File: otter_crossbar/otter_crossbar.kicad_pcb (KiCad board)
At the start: 4 copper layers, 166 x 19 mm, 13 parts, among them J1 Conn_02x12_Counter_Clockwise, J2 Conn_02x12_Counter_Clockwise, J3 Conn_02x12_Counter_Clockwise, J4 Conn_02x08_Odd_Even, J5 Conn_02x08_Odd_Even

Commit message: wip on crossbars
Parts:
- added J6: Conn_02x20_Odd_Even, custom:Samtec_MECF-20-0_-NP-L-DV_2x20_P1.27mm_Edge_mod, F.Cu at (0.00, -5.00)
- J4, J5: value Conn_02x08_Odd_Even -> Conn_02x12_Counter_Clockwise; footprint custom:Samtec_MECF-08-0_-NP-L-DV_2x08_P1.27mm_Edge_mod -> custom:PinSocket_2x12_P2.00mm_Vertical_EDGE
- moved J4 100.9 mm to (29.0, -19.9)
- moved J3 42.5 mm to (0.00, -19.9)
- moved J2 29.0 mm to (-29.0, -19.9)
- moved J5 19.7 mm to (58.0, -19.9)
- moved J1 15.5 mm to (-58.0, -19.9)
- moved H1 11.7 mm to (-91.7, -26.0)
- moved H2 11.7 mm to (-91.7, -13.0)
- moved H3 11.7 mm to (91.7, -26.0)
- moved H4 11.7 mm to (91.7, -13.0)
- moved JP1 11.7 mm to (-87.0, -25.9)
- moved JP2 11.7 mm to (-93.2, -18.9)
- moved JP3 11.7 mm to (87.2, -26.9)
- moved JP4 11.7 mm to (92.2, -18.4)
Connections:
- J1 pad 1: /C1 -> /E1
- J1 pad 11: /C6 -> /E6
- J1 pad 13: /C7 -> /E7
- J1 pad 17: /C9 -> /E9
- J1 pad 19: /C10 -> /E10
- J1 pad 21: /C11 -> /E2
- J1 pad 23: /C12 -> /E1
- J1 pad 3: /C2 -> /E2
- J1 pad 5: /C3 -> /E3
- J1 pad 7: /C4 -> /E4
- J2 pad 1: /B1 -> /D1
- J2 pad 11: /B6 -> /D6
- J2 pad 13: /B7 -> /D7
- J2 pad 17: /B9 -> /D9
- J2 pad 19: /B10 -> /D10
- J2 pad 21: /B11 -> /D2
- J2 pad 23: /B12 -> /D1
- J2 pad 3: /B2 -> /D2
- J2 pad 5: /B3 -> /D3
- J2 pad 7: /B4 -> /D4
- J3 pad 1: /A1 -> /C1
- J3 pad 11: /A6 -> /C6
- J3 pad 13: /A7 -> /C7
- J3 pad 17: /A9 -> /C9
- J3 pad 19: /A10 -> /C10
- J3 pad 21: /A11 -> /C2
- J3 pad 23: /A12 -> /C1
- J3 pad 3: /A2 -> /C2
- J3 pad 5: /A3 -> /C3
- J3 pad 7: /A4 -> /C4
- J4 pad 1: GND -> /B1
- J4 pad 10: /C7 -> (no net)
- J4 pad 11: /B12 -> /B6
- J4 pad 12: /C6 -> (no net)
- J4 pad 13: /C1 -> /B7
- J4 pad 14: /C4 -> (no net)
- J4 pad 15: /C2 -> (no net)
- J4 pad 16: /C3 -> (no net)
- J4 pad 2: /C12 -> (no net)
- J4 pad 3: /B7 -> /B2
- J4 pad 4: /C11 -> (no net)
- J4 pad 5: /B9 -> /B3
- J4 pad 6: /C10 -> (no net)
- J4 pad 7: /B10 -> /B4
- J4 pad 8: /C9 -> (no net)
- J4 pad 9: /B11 -> (no net)
- J5 pad 1: /A11 -> /A1
- J5 pad 10: /A4 -> (no net)
- J5 pad 11: /B4 -> /A6
- J5 pad 12: /A3 -> (no net)
- J5 pad 13: /B6 -> /A7
- J5 pad 14: /A2 -> (no net)
- J5 pad 15: GND -> (no net)
- J5 pad 16: /A1 -> (no net)
- J5 pad 2: /A10 -> (no net)
- J5 pad 3: /A12 -> /A2
- J5 pad 4: /A9 -> (no net)
- J5 pad 5: /B1 -> /A3
- J5 pad 6: /A7 -> (no net)
- J5 pad 7: /B2 -> /A4
- J5 pad 8: /A6 -> (no net)
- J5 pad 9: /B3 -> (no net)
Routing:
- net /E2: track 0.00 -> 96.2 mm, vias 0 -> 3
- net /E1: track 0.00 -> 93.0 mm, vias 0 -> 4
- net /B11: track 77.2 -> 0.00 mm, vias 2 -> 0
- net /B12: track 72.6 -> 0.00 mm, vias 2 -> 0
- net /D2: track 0.00 -> 67.8 mm, vias 0 -> 3
- net GND: track 182.1 -> 114.5 mm, vias 1 -> 6
- net /E10: track 0.00 -> 65.0 mm, vias 0 -> 2
- net /E9: track 0.00 -> 64.5 mm, vias 0 -> 2
- net /E7: track 0.00 -> 63.6 mm, vias 0 -> 2
- net /E6: track 0.00 -> 63.4 mm, vias 0 -> 2
- net /D1: track 0.00 -> 63.1 mm, vias 0 -> 4
- net /E4: track 0.00 -> 59.3 mm, vias 0 -> 2
- net /E3: track 0.00 -> 59.1 mm, vias 0 -> 2
- net /C3: track 75.9 -> 16.8 mm, vias 2 -> 1
- net /B6: track 93.1 -> 37.6 mm
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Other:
- board size 166 x 19 mm -> 189.4 x 19 mm

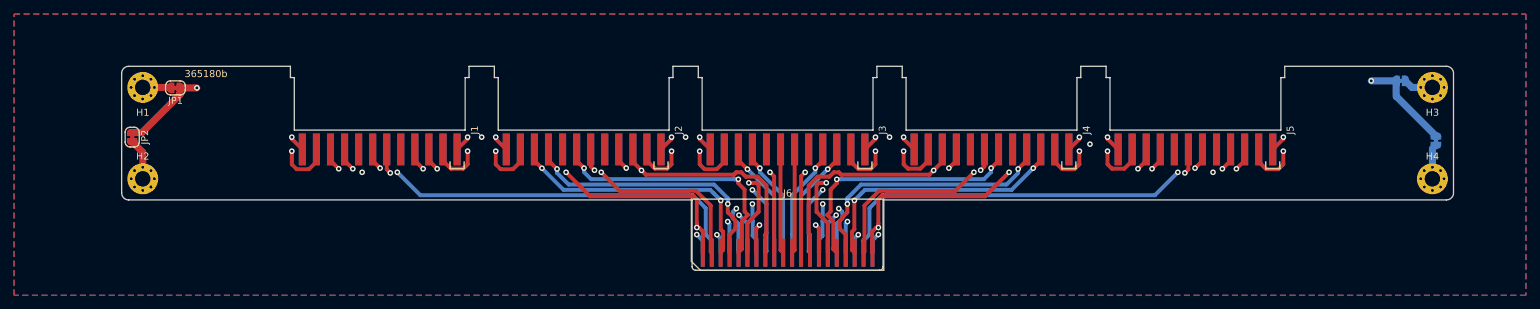
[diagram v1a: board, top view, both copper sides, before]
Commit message: otter crossbars shortened
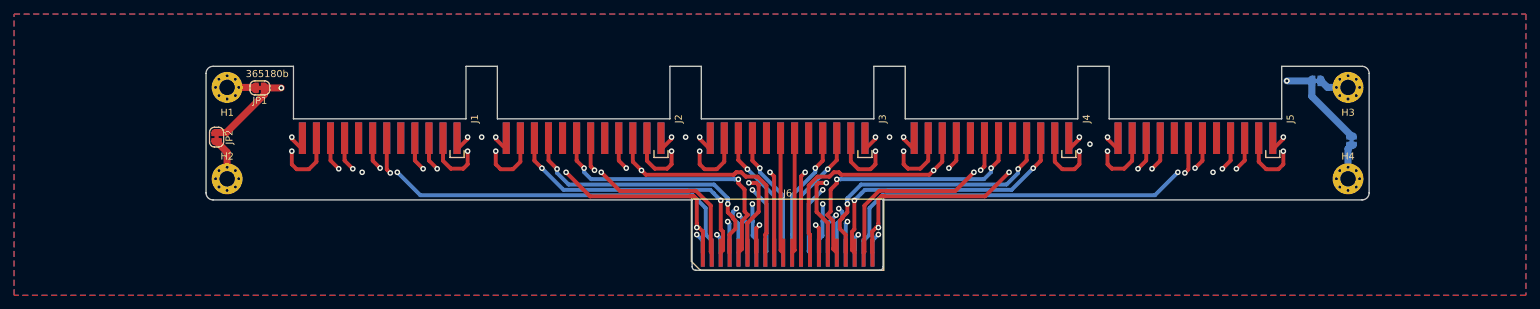
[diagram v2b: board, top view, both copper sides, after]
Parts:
- moved H1 12.0 mm to (-79.7, -26.0)
- moved H2 12.0 mm to (-79.7, -13.0)
- moved H3 12.0 mm to (79.7, -26.0)
- moved H4 12.0 mm to (79.7, -13.0)
- moved JP1 12.0 mm to (-75.0, -25.9)
- moved JP2 12.0 mm to (-81.2, -18.9)
- moved JP3 12.0 mm to (75.2, -26.9)
- moved JP4 12.0 mm to (80.2, -18.4)
- moved J1 1.60 mm to (-58.0, -21.5)
- moved J2 1.60 mm to (-29.0, -21.5)
- moved J3 1.60 mm to (0.00, -21.5)
- moved J4 1.60 mm to (29.0, -21.5)
- moved J5 1.60 mm to (58.0, -21.5)
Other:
- board size 189.4 x 19 mm -> 165.4 x 19 mm

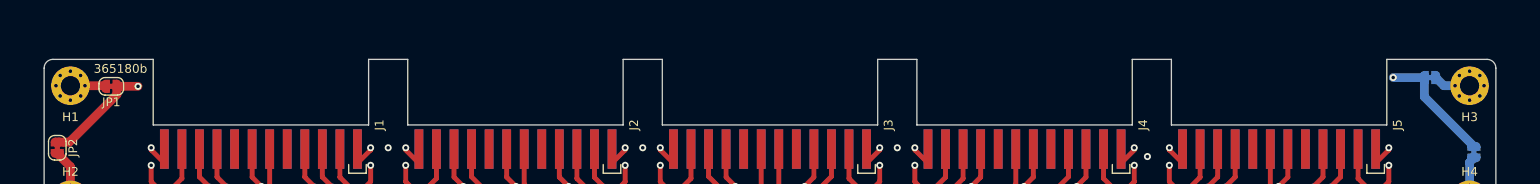
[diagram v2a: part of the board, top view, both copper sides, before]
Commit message: otter crossbar modified
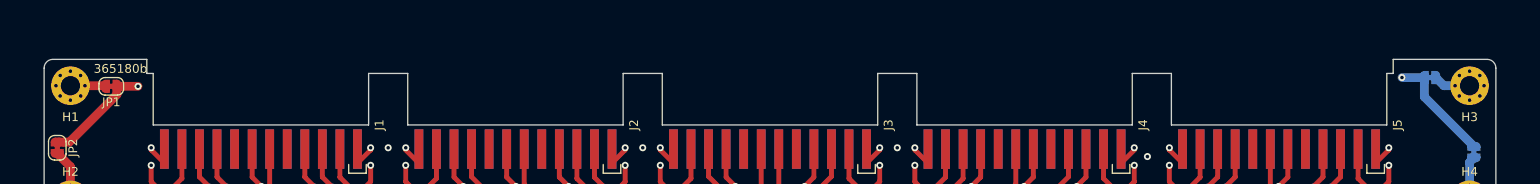
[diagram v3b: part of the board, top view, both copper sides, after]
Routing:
- net GND: track 114.5 -> 113.5 mm
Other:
- outline, holes or cut-outs redrawn
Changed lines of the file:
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@@
   (general
     (thickness 1.6)
-    (drawings 28)
+    (drawings 32)
     (tracks 631)
     (zones 0)
@@
       (net 38 /D1))
   )
+  (gr_line (start 71 -27.4) (end 71 -29) (layer Edge.Cuts) (width 0.05))
+  (gr_line (start -71 -29) (end -71 -27.4) (layer Edge.Cuts) (width 0.05))
+  (gr_line (start 70.27 -27.4) (end 71 -27.4) (layer Edge.Cuts) (width 0.05))
+  (gr_line (start -70.27 -27.4) (end -71 -27.4) (layer Edge.Cuts) (width 0.05))
   (gr_line (start -81.7 -10) (end -13.575 -10) (layer Edge.Cuts) (width 0.05))
-  (gr_line (start -70.27 -29) (end -81.7 -29) (layer Edge.Cuts) (width 0.05))
+  (gr_line (start -71 -29) (end -81.7 -29) (layer Edge.Cuts) (width 0.05))
   (gr_line (start 81.7 -10) (end 13.575 -10) (layer Edge.Cuts) (width 0.05))
-  (gr_line (start 70.27 -29) (end 81.7 -29) (layer Edge.Cuts) (width 0.05))
+  (gr_line (start 71 -29) (end 81.7 -29) (layer Edge.Cuts) (width 0.05))
   (gr_line (start 113 -9.5) (end -115 -9.5) (layer Dwgs.User) (width 0.15))
   (gr_line (start 113 2.5) (end -115 2.5) (layer Dwgs.User) (width 0.15))
-  (gr_line (start -45.73 -29) (end -41.27 -29) (layer Edge.Cuts) (width 0.05))
-  (gr_line (start -70.27 -21.53) (end -70.27 -29) (layer Edge.Cuts) (width 0.05))
-  (gr_line (start -45.73 -21.53) (end -45.73 -29) (layer Edge.Cuts) (width 0.05))
-  (gr_line (start 45.73 -21.53) (end 45.73 -29) (layer Edge.Cuts) (width 0.05))
-  (gr_line (start 41.27 -29) (end 45.73 -29) (layer Edge.Cuts) (width 0.05))
-  (gr_line (start 70.27 -21.53) (end 70.27 -29) (layer Edge.Cuts) (width 0.05))
-  (gr_line (start 16.73 -21.53) (end 16.73 -29) (layer Edge.Cuts) (width 0.05))
-  (gr_line (start 12.27 -29) (end 16.73 -29) (layer Edge.Cuts) (width 0.05))
-  (gr_line (start 41.27 -21.53) (end 41.27 -29) (layer Edge.Cuts) (width 0.05))
-  (gr_line (start -41.27 -21.53) (end -41.27 -29) (layer Edge.Cuts) (width 0.05))
-  (gr_line (start -16.73 -21.53) (end -16.73 -29) (layer Edge.Cuts) (width 0.05))
+  (gr_line (start -45.73 -27.4) (end -41.27 -27.4) (layer Edge.Cuts) (width 0.05))
+  (gr_line (start -70.27 -21.53) (end -70.27 -27.4) (layer Edge.Cuts) (width 0.05))
+  (gr_line (start -45.73 -21.53) (end -45.73 -27.4) (layer Edge.Cuts) (width 0.05))
+  (gr_line (start 45.73 -21.53) (end 45.73 -27.4) (layer Edge.Cuts) (width 0.05))
+  (gr_line (start 41.27 -27.4) (end 45.73 -27.4) (layer Edge.Cuts) (width 0.05))
+  (gr_line (start 70.27 -21.53) (end 70.27 -27.4) (layer Edge.Cuts) (width 0.05))
+  (gr_line (start 16.73 -21.53) (end 16.73 -27.4) (layer Edge.Cuts) (width 0.05))
+  (gr_line (start 12.27 -27.4) (end 16.73 -27.4) (layer Edge.Cuts) (width 0.05))
+  (gr_line (start 41.27 -21.53) (end 41.27 -27.4) (layer Edge.Cuts) (width 0.05))
+  (gr_line (start -41.27 -21.53) (end -41.27 -27.4) (layer Edge.Cuts) (width 0.05))
+  (gr_line (start -16.73 -21.53) (end -16.73 -27.4) (layer Edge.Cuts) (width 0.05))
   (gr_text 365180b (at -74 -27.93) (layer B.SilkS)
     (effects (font (size 1 1) (thickness 0.15)) (justify mirror))
@@
   (gr_arc (start 81.7 -11) (end 81.7 -10) (angle -90) (layer Edge.Cuts) (width 0.05))
   (gr_line (start 82.7 -11) (end 82.7 -28) (layer Edge.Cuts) (width 0.05))
-  (gr_line (start 12.27 -21.53) (end 12.27 -29) (layer Edge.Cuts) (width 0.05))
-  (gr_line (start -16.73 -29) (end -12.27 -29) (layer Edge.Cuts) (width 0.05))
-  (gr_line (start -12.27 -21.53) (end -12.27 -29) (layer Edge.Cuts) (width 0.05))
+  (gr_line (start 12.27 -21.53) (end 12.27 -27.4) (layer Edge.Cuts) (width 0.05))
+  (gr_line (start -16.73 -27.4) (end -12.27 -27.4) (layer Edge.Cuts) (width 0.05))
+  (gr_line (start -12.27 -21.53) (end -12.27 -27.4) (layer Edge.Cuts) (width 0.05))
   (gr_arc (start 81.7 -28) (end 82.7 -28) (angle -90) (layer Edge.Cuts) (width 0.05))
   (gr_arc (start -81.7 -28) (end -81.7 -29) (angle -90) (layer Edge.Cuts) (width 0.05))
@@
   (segment (start 80.2 -19.08) (end 74.55 -24.73) (width 1) (layer B.Cu) (net 29) (status 10))
   (via (at -72 -25.93) (size 0.8) (drill 0.4) (layers F.Cu B.Cu) (net 29))
-  (via (at 71 -26.93) (size 0.8) (drill 0.4) (layers F.Cu B.Cu) (net 29))
-  (segment (start 74.55 -26.93) (end 71 -26.93) (width 1) (layer B.Cu) (net 29) (status 10))
   (segment (start -72 -25.93) (end -74.4 -25.93) (width 1) (layer F.Cu) (net 29) (status 20))
   (via (at 43 -17.93) (size 0.8) (drill 0.4) (layers F.Cu B.Cu) (net 29))
@@
   (segment (start 15.5 -17.93) (end 43 -17.93) (width 0.56) (layer In2.Cu) (net 29))
   (segment (start 14.5 -18.93) (end 15.5 -17.93) (width 0.56) (layer In2.Cu) (net 29))
+  (segment (start 74.55 -26.93) (end 72 -26.93) (width 1) (layer B.Cu) (net 29))
+  (via (at 72 -26.93) (size 0.8) (drill 0.4) (layers F.Cu B.Cu) (net 29))
   (via (at -60.5 -13.93) (size 0.8) (drill 0.4) (layers F.Cu B.Cu) (net 30))
   (segment (start -70.5 -18.68) (end -69 -17.18) (width 0.56) (layer F.Cu) (net 30) (status 20))

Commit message: update silk
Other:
- board text added: "6c4861d"
- board text removed: "365180b"
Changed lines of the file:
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@@
   (gr_line (start -41.27 -21.53) (end -41.27 -27.4) (layer Edge.Cuts) (width 0.05))
   (gr_line (start -16.73 -21.53) (end -16.73 -27.4) (layer Edge.Cuts) (width 0.05))
-  (gr_text 365180b (at -74 -27.93) (layer B.SilkS)
+  (gr_text 6c4861d (at -74.5 -28) (layer B.SilkS)
     (effects (font (size 1 1) (thickness 0.15)) (justify mirror))
   )
-  (gr_text 365180b (at -74 -27.93) (layer F.SilkS)
+  (gr_text 6c4861d (at -74.5 -27.93) (layer F.SilkS)
     (effects (font (size 1 1) (thickness 0.15)))
   )

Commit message: start baseboard
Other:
- board text added: "A"
- board text added: "B"
- board text added: "C"
- board text added: "D"
- board text added: "E"
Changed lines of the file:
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@@
   (general
     (thickness 1.6)
-    (drawings 32)
+    (drawings 42)
     (tracks 631)
     (zones 0)
@@
       (effects (font (size 1 1) (thickness 0.15)))
     )
-    (fp_text value Conn_02x12_Counter_Clockwise (at -13.5 0 270) (layer F.Fab)
+    (fp_text value Conn_02x12_Counter_Clockwise (at -13.5 0 270) (layer F.Fab) hide
       (effects (font (size 1 1) (thickness 0.15)))
     )
@@
       (effects (font (size 1 1) (thickness 0.15)))
     )
-    (fp_text value Conn_02x12_Counter_Clockwise (at -13.5 0 270) (layer F.Fab)
+    (fp_text value Conn_02x12_Counter_Clockwise (at -13.5 0 270) (layer F.Fab) hide
       (effects (font (size 1 1) (thickness 0.15)))
     )
@@
     (tags "conn samtec card-edge high-speed")
     (attr virtual)
-    (fp_text reference J6 (at 0 -5.95) (layer F.SilkS)
+    (fp_text reference J6 (at -12.5 -6) (layer F.SilkS)
       (effects (font (size 1 1) (thickness 0.15)))
     )
@@
       (net 38 /D1))
   )
+  (gr_text E (at -58.5 -11.5) (layer B.SilkS)
+    (effects (font (size 1 1) (thickness 0.15)) (justify mirror))
+  )
+  (gr_text D (at -29 -11.5) (layer B.SilkS)
+    (effects (font (size 1 1) (thickness 0.15)) (justify mirror))
+  )
+  (gr_text C (at 0 -13) (layer B.SilkS)
+    (effects (font (size 1 1) (thickness 0.15)) (justify mirror))
+  )
+  (gr_text B (at 29.5 -12) (layer B.SilkS)
+    (effects (font (size 1 1) (thickness 0.15)) (justify mirror))
+  )
+  (gr_text A (at 58 -12) (layer B.SilkS)
+    (effects (font (size 1 1) (thickness 0.15)) (justify mirror))
+  )
+  (gr_text A (at 58 -12) (layer F.SilkS)
+    (effects (font (size 1 1) (thickness 0.15)))
+  )
+  (gr_text B (at 29.5 -12) (layer F.SilkS)
+    (effects (font (size 1 1) (thickness 0.15)))
+  )
+  (gr_text C (at 0 -13) (layer F.SilkS)
+    (effects (font (size 1 1) (thickness 0.15)))
+  )
+  (gr_text D (at -29 -11.5) (layer F.SilkS)
+    (effects (font (size 1 1) (thickness 0.15)))
+  )
+  (gr_text E (at -58.5 -11.5) (layer F.SilkS)
+    (effects (font (size 1 1) (thickness 0.15)))
+  )
   (gr_line (start 71 -27.4) (end 71 -29) (layer Edge.Cuts) (width 0.05))

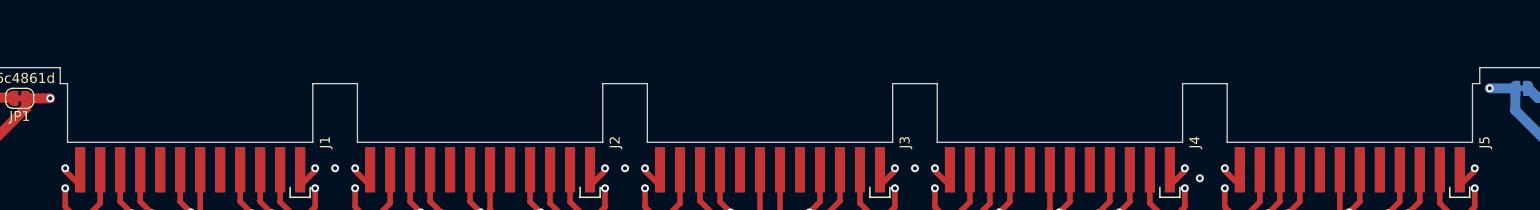
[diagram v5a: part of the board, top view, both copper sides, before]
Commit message: fix lim baseboard bug
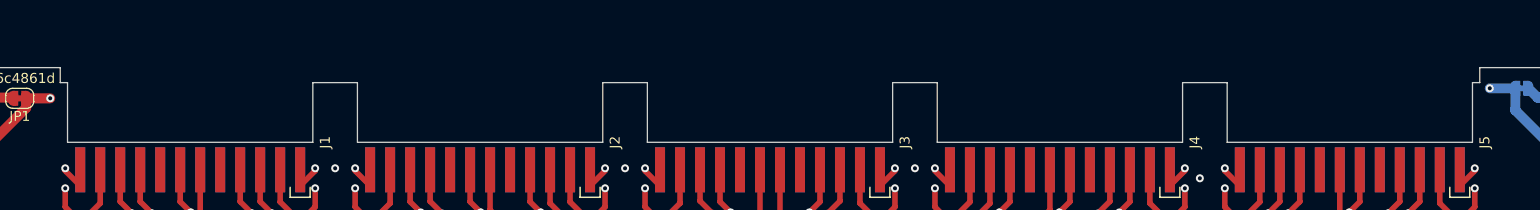
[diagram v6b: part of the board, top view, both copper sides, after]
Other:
- outline, holes or cut-outs redrawn
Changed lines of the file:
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@@
     (effects (font (size 1 1) (thickness 0.15)))
   )
-  (gr_line (start 71 -27.4) (end 71 -29) (layer Edge.Cuts) (width 0.05))
-  (gr_line (start -71 -29) (end -71 -27.4) (layer Edge.Cuts) (width 0.05))
-  (gr_line (start 70.27 -27.4) (end 71 -27.4) (layer Edge.Cuts) (width 0.05))
-  (gr_line (start -70.27 -27.4) (end -71 -27.4) (layer Edge.Cuts) (width 0.05))
+  (gr_line (start 71 -27.5) (end 71 -29) (layer Edge.Cuts) (width 0.05))
+  (gr_line (start -71 -29) (end -71 -27.5) (layer Edge.Cuts) (width 0.05))
+  (gr_line (start 70.27 -27.5) (end 71 -27.5) (layer Edge.Cuts) (width 0.05))
+  (gr_line (start -70.27 -27.5) (end -71 -27.5) (layer Edge.Cuts) (width 0.05))
   (gr_line (start -81.7 -10) (end -13.575 -10) (layer Edge.Cuts) (width 0.05))
   (gr_line (start -71 -29) (end -81.7 -29) (layer Edge.Cuts) (width 0.05))
@@
   (gr_line (start 113 -9.5) (end -115 -9.5) (layer Dwgs.User) (width 0.15))
   (gr_line (start 113 2.5) (end -115 2.5) (layer Dwgs.User) (width 0.15))
-  (gr_line (start -45.73 -27.4) (end -41.27 -27.4) (layer Edge.Cuts) (width 0.05))
-  (gr_line (start -70.27 -21.53) (end -70.27 -27.4) (layer Edge.Cuts) (width 0.05))
-  (gr_line (start -45.73 -21.53) (end -45.73 -27.4) (layer Edge.Cuts) (width 0.05))
-  (gr_line (start 45.73 -21.53) (end 45.73 -27.4) (layer Edge.Cuts) (width 0.05))
-  (gr_line (start 41.27 -27.4) (end 45.73 -27.4) (layer Edge.Cuts) (width 0.05))
-  (gr_line (start 70.27 -21.53) (end 70.27 -27.4) (layer Edge.Cuts) (width 0.05))
-  (gr_line (start 16.73 -21.53) (end 16.73 -27.4) (layer Edge.Cuts) (width 0.05))
-  (gr_line (start 12.27 -27.4) (end 16.73 -27.4) (layer Edge.Cuts) (width 0.05))
-  (gr_line (start 41.27 -21.53) (end 41.27 -27.4) (layer Edge.Cuts) (width 0.05))
-  (gr_line (start -41.27 -21.53) (end -41.27 -27.4) (layer Edge.Cuts) (width 0.05))
-  (gr_line (start -16.73 -21.53) (end -16.73 -27.4) (layer Edge.Cuts) (width 0.05))
+  (gr_line (start -45.73 -27.5) (end -41.27 -27.5) (layer Edge.Cuts) (width 0.05))
+  (gr_line (start -70.27 -21.53) (end -70.27 -27.5) (layer Edge.Cuts) (width 0.05))
+  (gr_line (start -45.73 -21.53) (end -45.73 -27.5) (layer Edge.Cuts) (width 0.05))
+  (gr_line (start 45.73 -21.53) (end 45.73 -27.5) (layer Edge.Cuts) (width 0.05))
+  (gr_line (start 41.27 -27.5) (end 45.73 -27.5) (layer Edge.Cuts) (width 0.05))
+  (gr_line (start 70.27 -21.53) (end 70.27 -27.5) (layer Edge.Cuts) (width 0.05))
+  (gr_line (start 16.73 -21.53) (end 16.73 -27.5) (layer Edge.Cuts) (width 0.05))
+  (gr_line (start 12.27 -27.5) (end 16.73 -27.5) (layer Edge.Cuts) (width 0.05))
+  (gr_line (start 41.27 -21.53) (end 41.27 -27.5) (layer Edge.Cuts) (width 0.05))
+  (gr_line (start -41.27 -21.53) (end -41.27 -27.5) (layer Edge.Cuts) (width 0.05))
+  (gr_line (start -16.73 -21.53) (end -16.73 -27.5) (layer Edge.Cuts) (width 0.05))
   (gr_text 6c4861d (at -74.5 -28) (layer B.SilkS)
     (effects (font (size 1 1) (thickness 0.15)) (justify mirror))
@@
   (gr_arc (start 81.7 -11) (end 81.7 -10) (angle -90) (layer Edge.Cuts) (width 0.05))
   (gr_line (start 82.7 -11) (end 82.7 -28) (layer Edge.Cuts) (width 0.05))
-  (gr_line (start 12.27 -21.53) (end 12.27 -27.4) (layer Edge.Cuts) (width 0.05))
-  (gr_line (start -16.73 -27.4) (end -12.27 -27.4) (layer Edge.Cuts) (width 0.05))
-  (gr_line (start -12.27 -21.53) (end -12.27 -27.4) (layer Edge.Cuts) (width 0.05))
+  (gr_line (start 12.27 -21.53) (end 12.27 -27.5) (layer Edge.Cuts) (width 0.05))
+  (gr_line (start -16.73 -27.5) (end -12.27 -27.5) (layer Edge.Cuts) (width 0.05))
+  (gr_line (start -12.27 -21.53) (end -12.27 -27.5) (layer Edge.Cuts) (width 0.05))
   (gr_arc (start 81.7 -28) (end 82.7 -28) (angle -90) (layer Edge.Cuts) (width 0.05))
   (gr_arc (start -81.7 -28) (end -81.7 -29) (angle -90) (layer Edge.Cuts) (width 0.05))
